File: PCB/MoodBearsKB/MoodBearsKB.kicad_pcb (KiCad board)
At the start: 2 copper layers, 266.5 x 94.5 mm, 104 parts, among them J1 MJ-4PP-9, J2 MJ-4PP-9, U1 xiao-ble, U2 xiao-ble

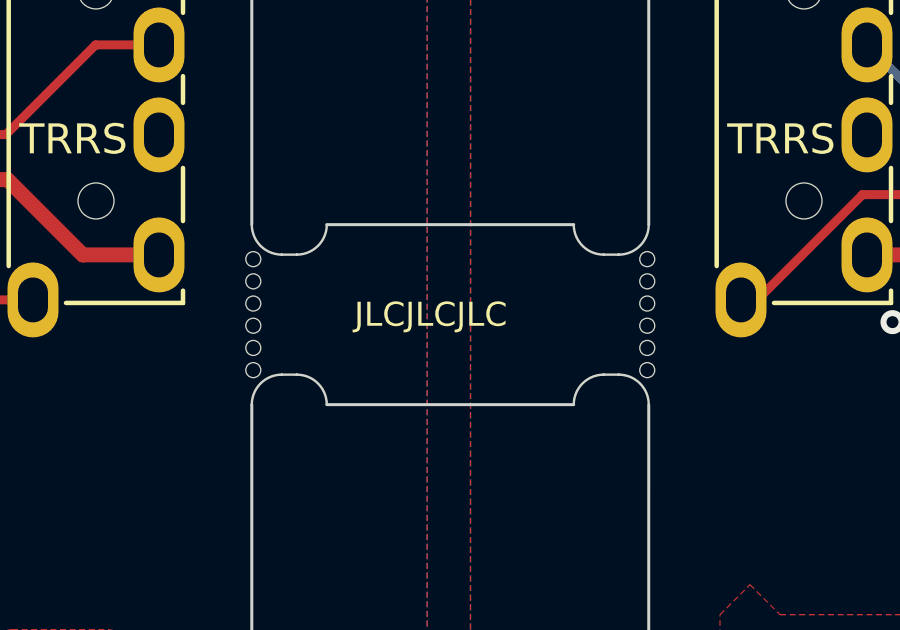
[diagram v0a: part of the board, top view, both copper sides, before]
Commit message: added pcbway Prod Files and specified order number location
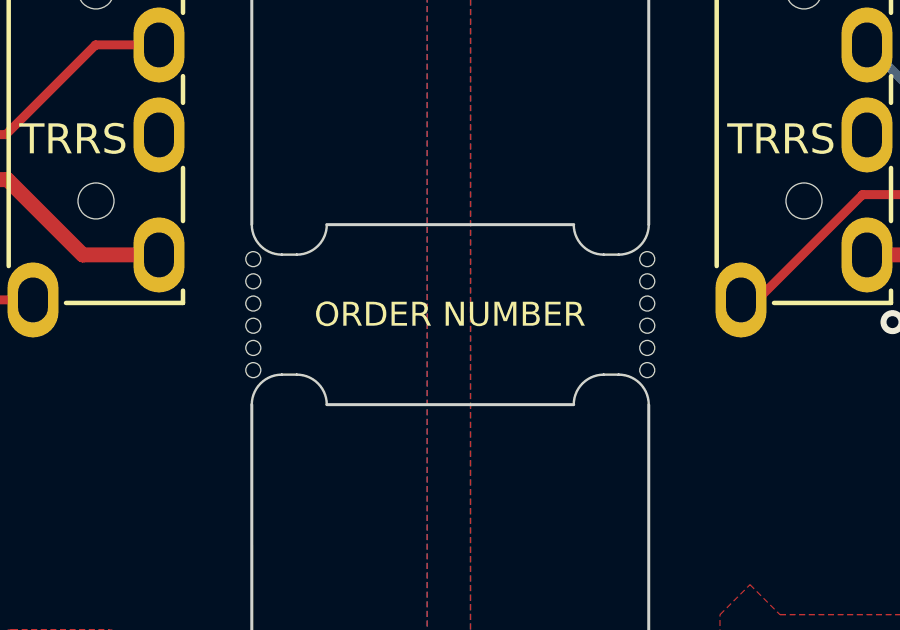
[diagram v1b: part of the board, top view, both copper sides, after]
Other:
- board text added: "ORDER NUMBER"
- board text removed: "JLCJLCJLC"
